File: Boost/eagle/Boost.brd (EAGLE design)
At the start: 100 x 80 mm, 17 parts, among them X1 22-23-2051

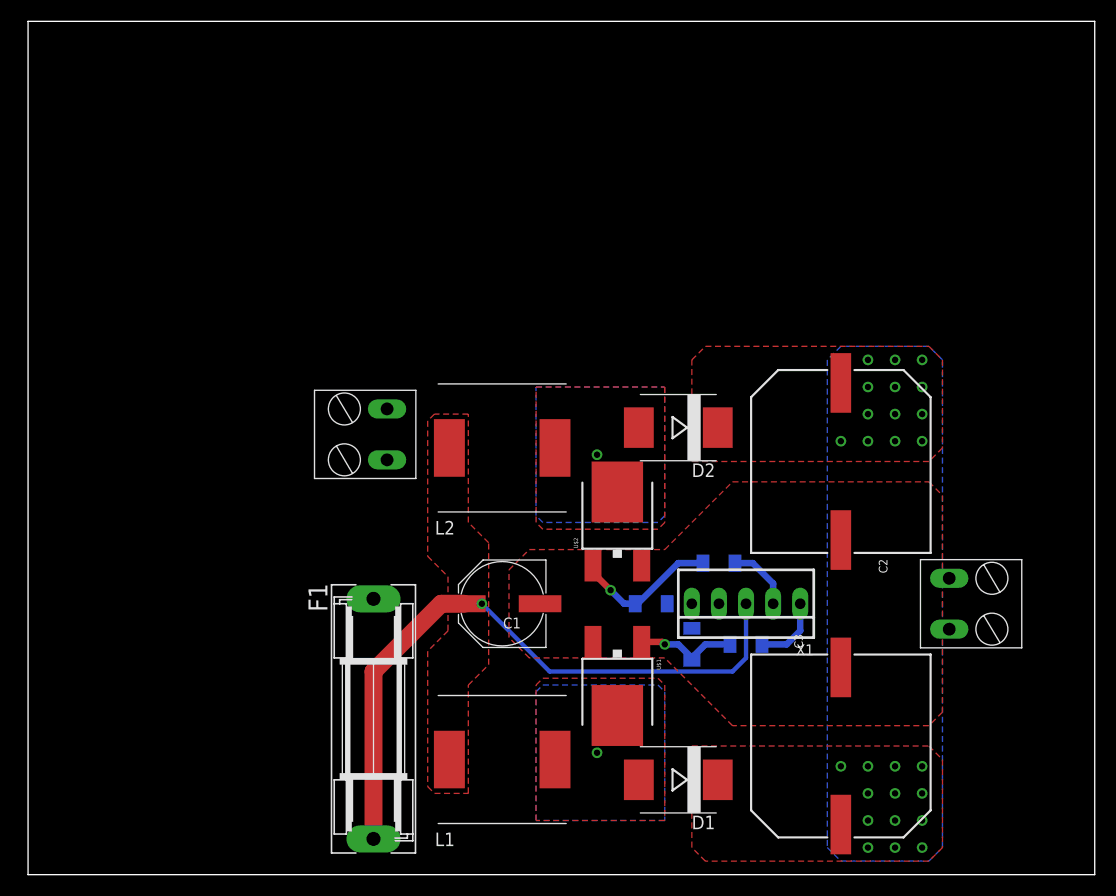
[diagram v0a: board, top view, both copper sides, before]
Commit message: updated boost converter layout
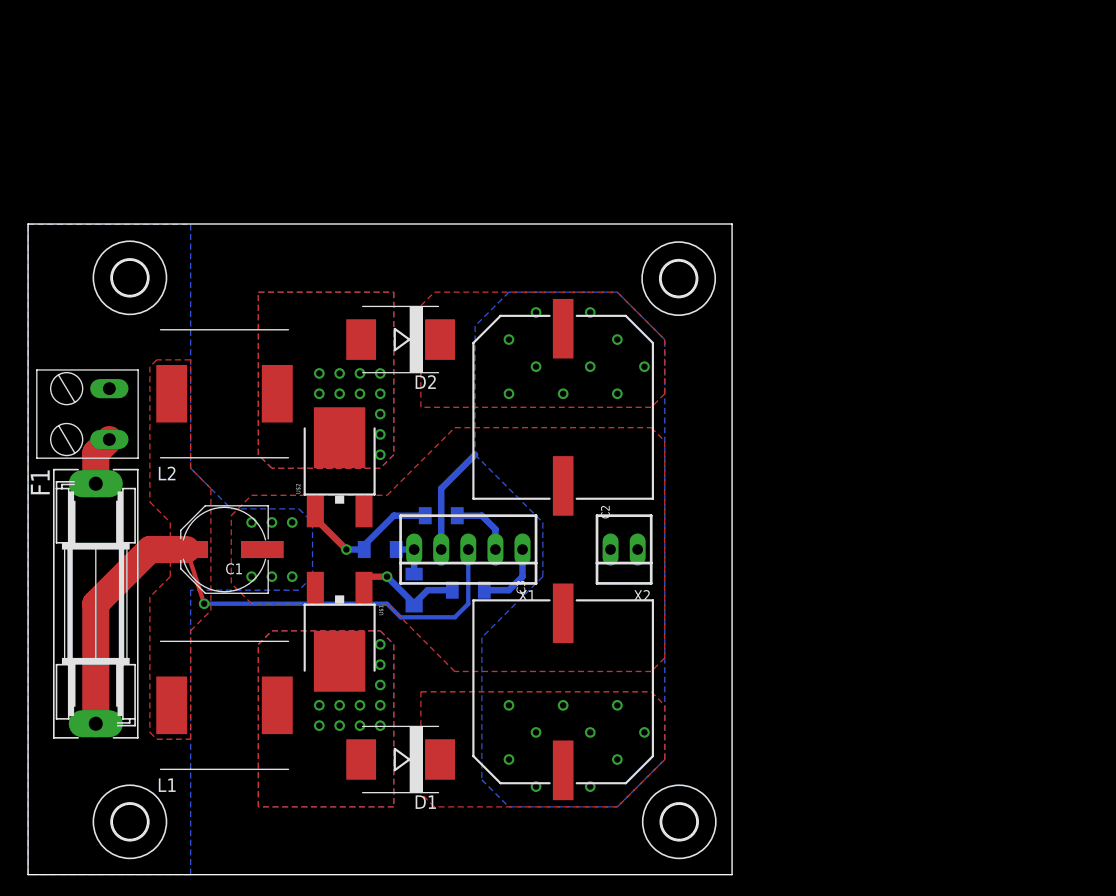
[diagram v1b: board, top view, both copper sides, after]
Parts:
- removed U$4: RIACON-2, ppst002:RIACON2
- added H1, H2, H3, H4: MOUNT-HOLE3.3, holes:3,3
- added X2: 22-23-2021, con-molex:22-23-2021
- moved F1 28.2 mm to (6.35, 25.4)
- moved D2 27.3 mm to (34.9, 50.2)
- moved C1 26.5 mm to (18.4, 30.5)
- moved C2 26.5 mm to (50.2, 42.5)
- moved C3 26.5 mm to (50.2, 18.4)
- moved L1 26.5 mm to (18.4, 15.9)
- moved L2 26.5 mm to (18.4, 45.1)
- moved R2 26.5 mm to (41.3, 26.7)
- moved U$2 26.5 mm to (25.4, 31.8)
- moved X1 26.5 mm to (41.3, 30.5)
- moved R4 26.5 mm to (36.2, 26.7)
- moved U$1 26.5 mm to (33.0, 29.2)
- moved R1 26.4 mm to (38.7, 33.7)
- moved D1 26.1 mm to (34.9, 10.8)
- moved U$3 26.1 mm to (1.27, 38.7)
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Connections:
- net GND: now also X2.2; no longer U$4.P$2
- net UOUT: now also X2.1; no longer U$4.P$1
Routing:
- net UOUT: track 0.00 -> 10.2 mm, vias 19 -> 20
- net N$5: track 0.00 -> 4.67 mm
- net GND: track 0.00 -> 3.98 mm, vias 0 -> 6
- net UIN: track 61.5 -> 58.1 mm
- net N$6: track 10.2 -> 11.7 mm
- added copper zone on layer 16, net GND
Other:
- board size 100 x 80 mm -> 66 x 61 mm
